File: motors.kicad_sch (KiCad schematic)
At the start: 1 part

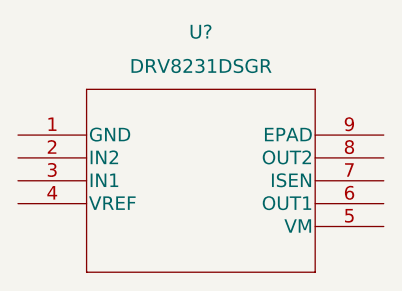
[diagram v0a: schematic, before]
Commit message: Added MAX20077 for 6V output
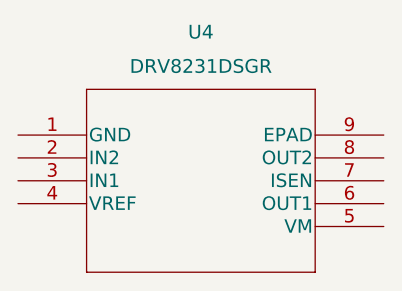
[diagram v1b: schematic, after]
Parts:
- U4: renamed from U?; footprint Package_SON:WSON-8-1EP_2x2mm_P0.5mm_EP0.9x1.6mm -> DRV8231ADSGR:SON50P200X200X80-9N
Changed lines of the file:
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@@
   (symbol (lib_id "DRV8321:DRV8231DSGR") (at 36.83 40.64 0) (unit 1)
     (in_bom yes) (on_board yes) (fields_autoplaced)
-    (property "Reference" "U?" (id 0) (at 57.15 29.21 0)
+    (property "Reference" "U4" (id 0) (at 57.15 29.21 0)
       (effects (font (size 1.524 1.524)))
     )
@@
       (effects (font (size 1.524 1.524)))
     )
-    (property "Footprint" "Package_SON:WSON-8-1EP_2x2mm_P0.5mm_EP0.9x1.6mm" (id 2) (at 57.15 34.544 0)
+    (property "Footprint" "DRV8231ADSGR:SON50P200X200X80-9N" (id 2) (at 57.15 34.544 0)
       (effects (font (size 1.524 1.524)) hide)
     )
